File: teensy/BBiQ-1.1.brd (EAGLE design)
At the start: 61.5 x 58.1 mm, 29 parts, among them IC1 ESP-WROOM-02, J1 MJ-2506N, J2 MJ-2506N, J3 MJ-2506N, J4 MJ-2506N, T1 2N3904

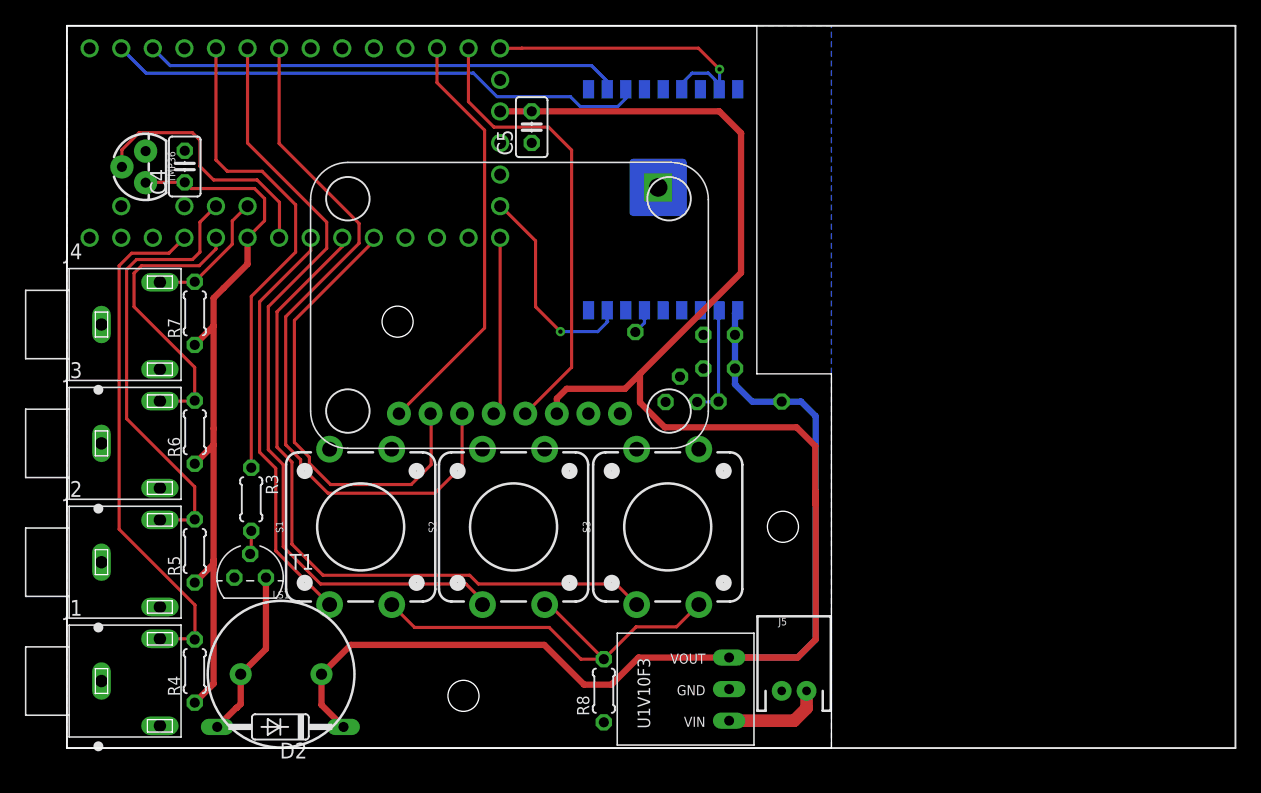
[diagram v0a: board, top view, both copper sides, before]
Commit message: new board with teensyview
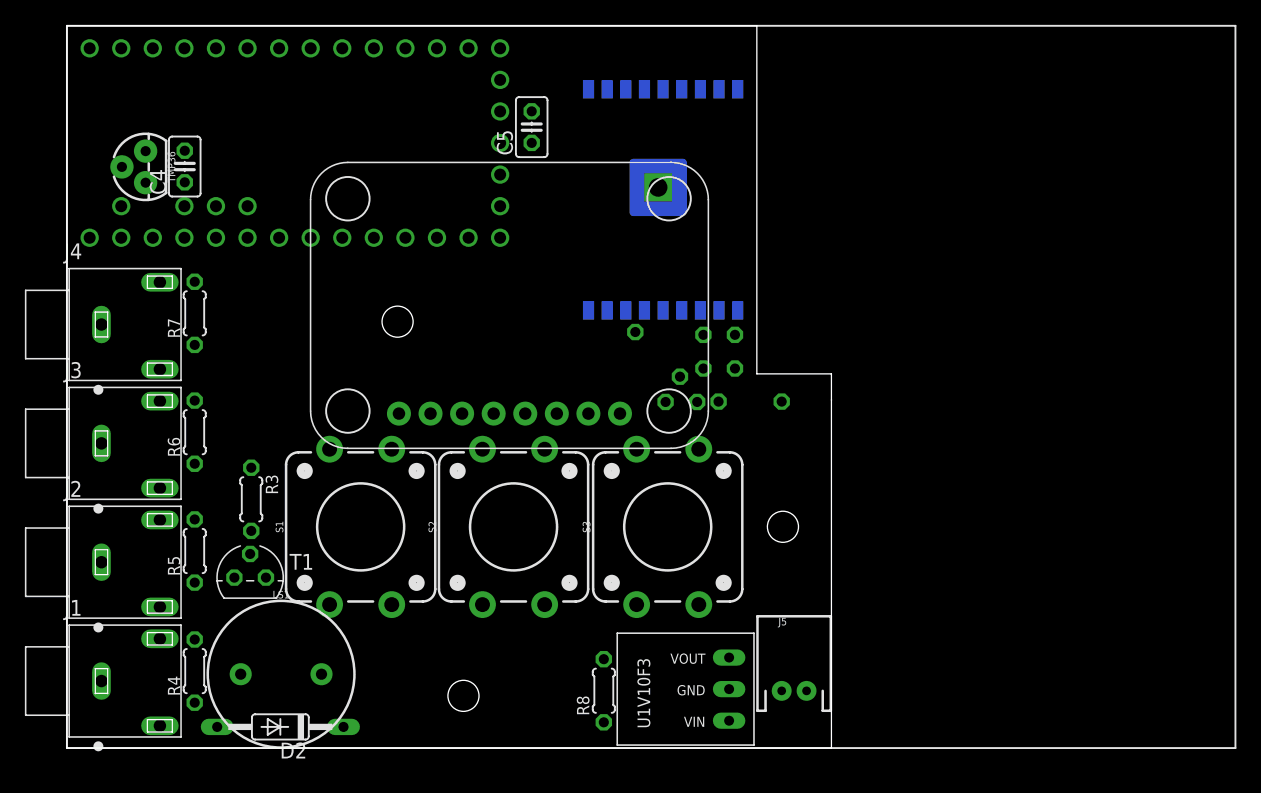
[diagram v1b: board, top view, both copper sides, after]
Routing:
- net +3V3: track 173.8 -> 0.00 mm
- net BUTTON_1: track 63.3 -> 0.00 mm
- net PROBE_PWR: track 59.7 -> 0.00 mm
- net OLED_DC: track 58.2 -> 0.00 mm
- net BUTTON_2: track 57.1 -> 0.00 mm
- net ESP_TX: track 43.5 -> 0.00 mm
- net PROBE_0: track 41.6 -> 0.00 mm
- net BUZZER: track 39.5 -> 0.00 mm
- net ESP_RX: track 38.3 -> 0.00 mm
- net OLED_DATA: track 37.0 -> 0.00 mm
- net OLED_RST: track 36.6 -> 0.00 mm
- net PROBE_1: track 35.9 -> 0.00 mm
- net N$7: track 34.9 -> 0.00 mm
- net OLED_CS: track 33.8 -> 0.00 mm
- net BUTTON_0: track 33.5 -> 0.00 mm
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- removed copper zone on layer 16, net GND
